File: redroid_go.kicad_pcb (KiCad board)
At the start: 2 copper layers, 70 x 95 mm, 100 parts, among them J1 USB4105-GF-A, J2 5051101892, J3 Conn_01x02_Pin, J4 Conn_01x10_Pin, Q1 UMH3N, Q2 PMOS, Q3 UMH3N, SW1 UP, SW10 A, SW11 SW_SPDT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

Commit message: Change DPAD resistors
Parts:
- R11, R12, R13, R14: value 10k -> 100k
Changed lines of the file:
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@@
 			)
 		)
-		(property "Value" "10k"
+		(property "Value" "100k"
 			(at 0 -1.43 0)
 			(layer "B.Fab")
@@
 			)
 		)
-		(property "Value" "10k"
+		(property "Value" "100k"
 			(at 0 -1.43 0)
 			(layer "B.Fab")
@@
 			)
 		)
-		(property "Value" "10k"
+		(property "Value" "100k"
 			(at 0 -1.43 0)
 			(layer "B.Fab")
@@
 			)
 		)
-		(property "Value" "10k"
+		(property "Value" "100k"
 			(at 0 -1.43 0)
 			(layer "B.Fab")

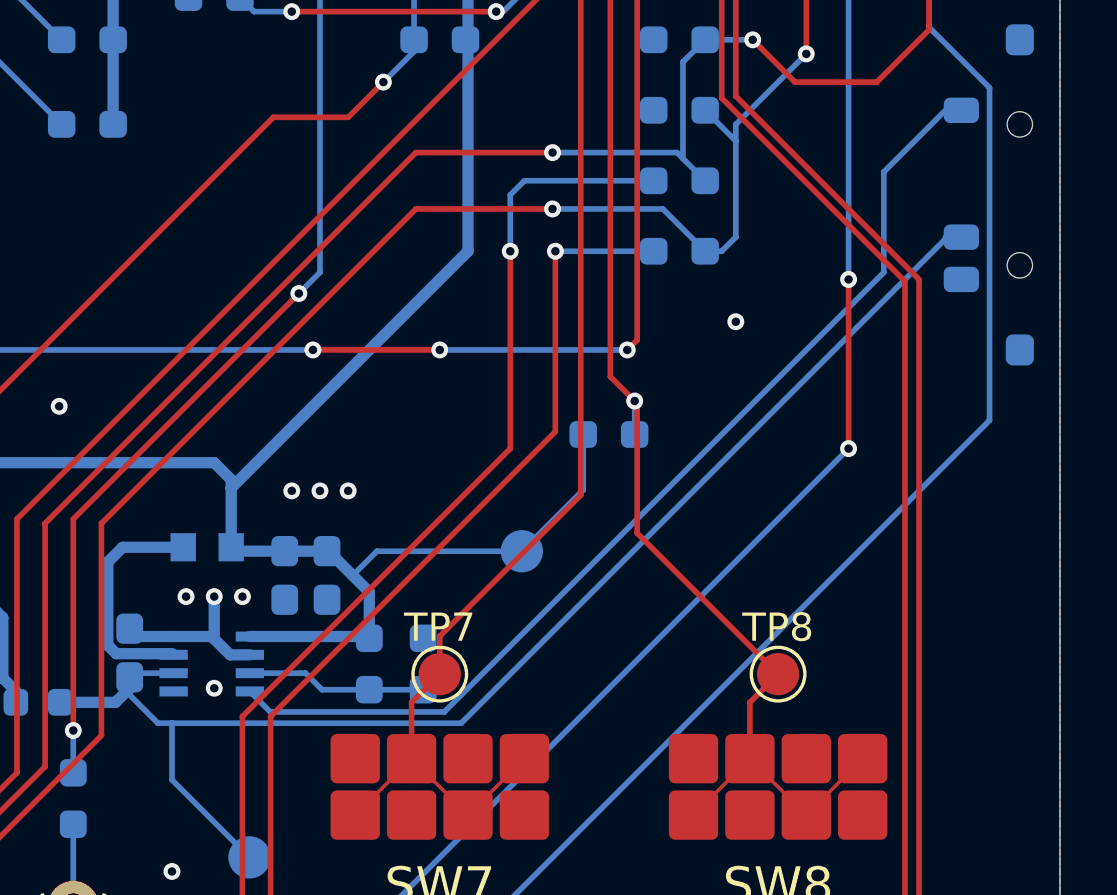
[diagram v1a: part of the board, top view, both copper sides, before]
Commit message: Fix filled zones
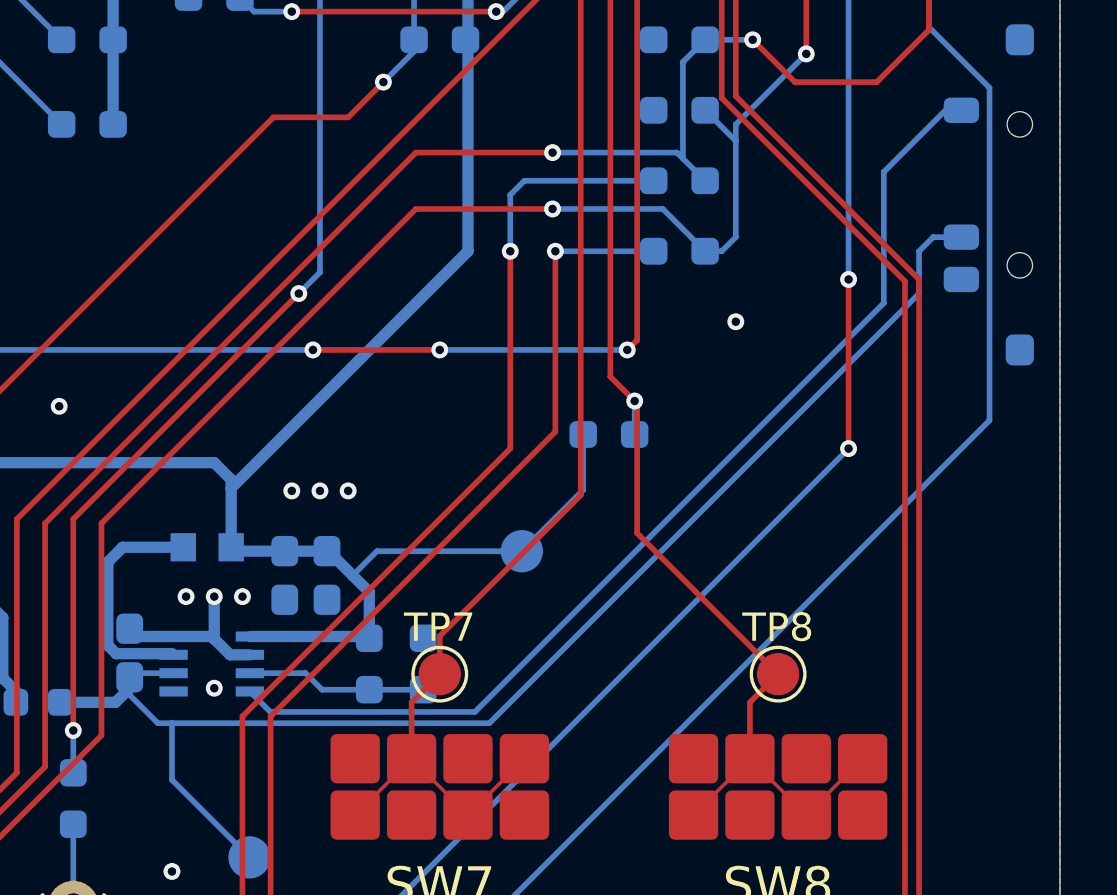
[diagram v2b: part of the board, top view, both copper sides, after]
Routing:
- net Net-(SW11-B): track 47.7 -> 49.1 mm
- net Net-(SW11-A): track 35.9 -> 36.5 mm
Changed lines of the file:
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@@
 	)
 	(segment
-		(start 194.4375 85.5625)
-		(end 177.259551 102.740449)
+		(start 178.259551 102.740449)
+		(end 167 102.740449)
 		(width 0.2)
 		(layer "B.Cu")
@@
 	)
 	(segment
-		(start 177.259551 102.740449)
+		(start 167 104.75)
 		(end 167 102.740449)
 		(width 0.2)
@@
 	)
 	(segment
-		(start 167 104.75)
-		(end 167 102.740449)
+		(start 193.5 86)
+		(end 193.5 87.5)
 		(width 0.2)
 		(layer "B.Cu")
@@
 	)
 	(segment
+		(start 195 85.5)
+		(end 194 85.5)
+		(width 0.2)
+		(layer "B.Cu")
+		(net 4)
+	)
+	(segment
 		(start 167.057201 100.96545)
 		(end 165.64705 100.96545)
@@
 	)
 	(segment
-		(start 194.4375 85.5)
-		(end 194.4375 85.5625)
+		(start 165.64705 100.96545)
+		(end 165.5 101.1125)
 		(width 0.2)
 		(layer "B.Cu")
@@
 	)
 	(segment
-		(start 165.64705 100.96545)
-		(end 165.5 101.1125)
+		(start 193.5 87.5)
+		(end 178.259551 102.740449)
 		(width 0.2)
 		(layer "B.Cu")
@@
 	)
 	(segment
+		(start 194 85.5)
+		(end 193.5 86)
+		(width 0.2)
+		(layer "B.Cu")
+		(net 4)
+	)
+	(segment
 		(start 136.5 52)
 		(end 137 51.5)
@@
 	)
 	(segment
-		(start 192.25 83.1875)
-		(end 192.25 86.75)
+		(start 177.746934 102.340449)
+		(end 170.488698 102.340449)
 		(width 0.2)
 		(layer "B.Cu")
@@
 	)
 	(segment
-		(start 170.488698 102.340449)
-		(end 169.763697 101.615448)
+		(start 194.4375 81)
+		(end 192.25 83.1875)
 		(width 0.2)
 		(layer "B.Cu")
@@
 	)
 	(segment
-		(start 192.25 86.75)
-		(end 176.659551 102.340449)
+		(start 170.488698 102.340449)
+		(end 169.763697 101.615448)
 		(width 0.2)
 		(layer "B.Cu")
@@
 	)
 	(segment
-		(start 194.4375 81)
-		(end 192.25 83.1875)
+		(start 192.25 87.837383)
+		(end 177.746934 102.340449)
 		(width 0.2)
 		(layer "B.Cu")
@@
 	)
 	(segment
-		(start 176.659551 102.340449)
-		(end 170.488698 102.340449)
+		(start 192.25 83.1875)
+		(end 192.25 87.837383)
 		(width 0.2)
 		(layer "B.Cu")

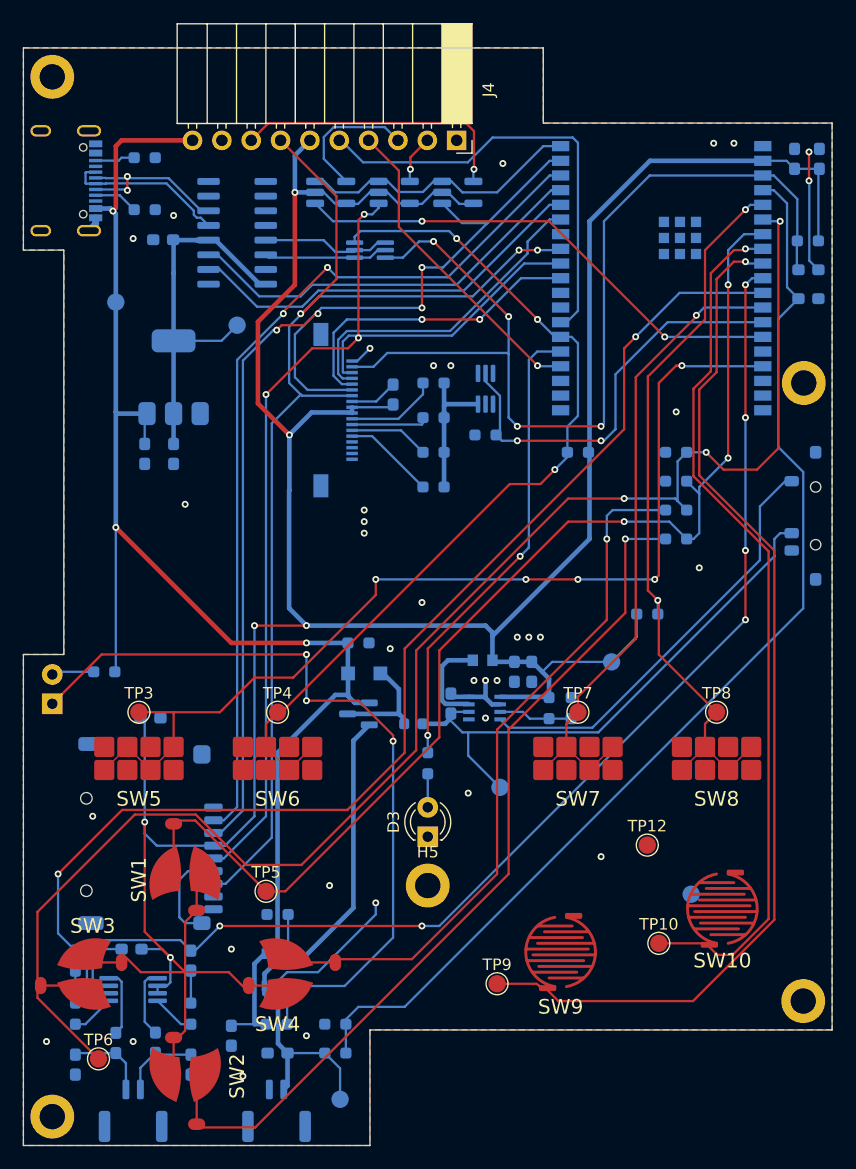
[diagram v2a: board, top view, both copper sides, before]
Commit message: Move menu buttons
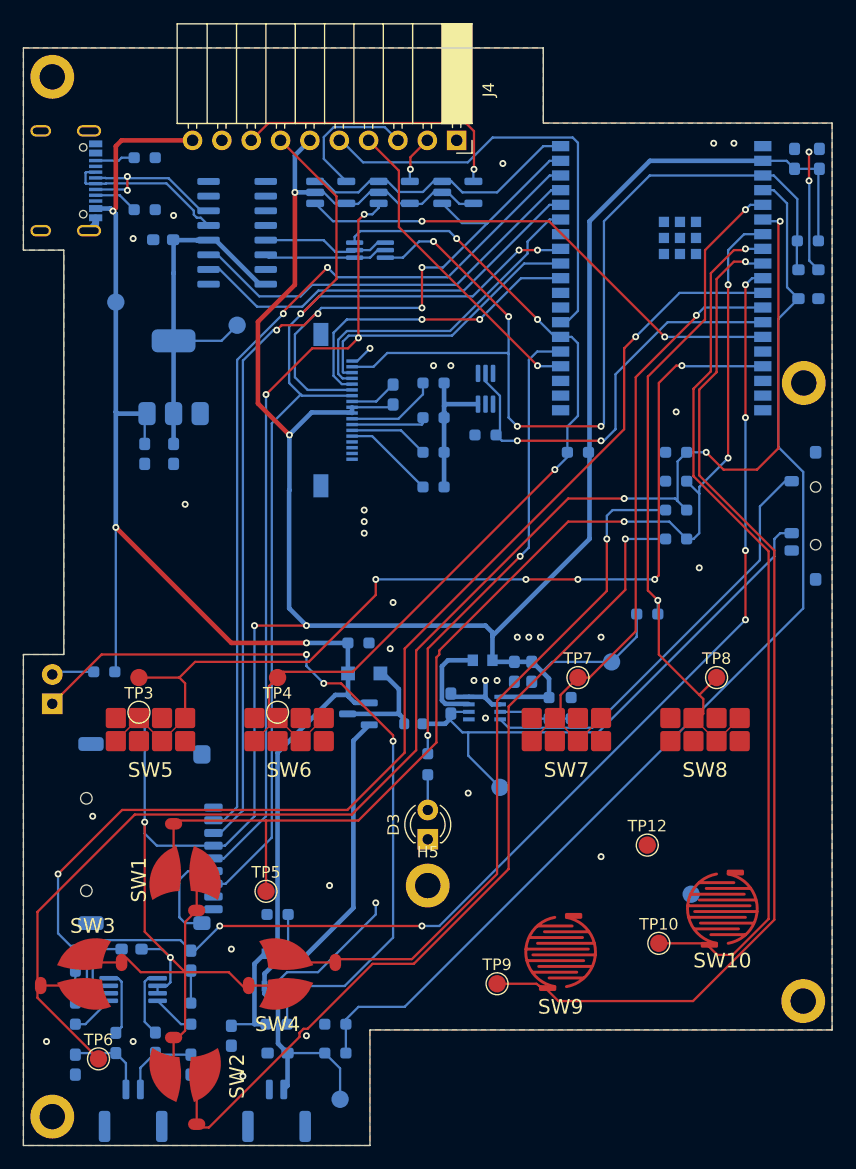
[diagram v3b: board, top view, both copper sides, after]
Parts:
- moved TP7 3.00 mm to (176.5, 98.0)
- moved TP8 3.00 mm to (188.5, 98.0)
- moved SW5 2.69 mm to (139.5, 102.5)
- moved SW6 2.69 mm to (151.5, 102.5)
- moved SW7 2.69 mm to (175.5, 102.5)
- moved SW8 2.69 mm to (187.5, 102.5)
- moved D3 0.23 mm to (163.5, 112.0)
- moved R18 0.09 mm to (163.5, 105.5)
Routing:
- net IO34: track 129.6 -> 126.0 mm
- net Net-(D2-K): track 68.3 -> 66.5 mm
- net IO27: track 47.9 -> 46.2 mm
- net IO0: track 72.2 -> 70.8 mm
- net IO39: track 55.6 -> 54.3 mm
- net IO35: track 96.9 -> 98.1 mm
- net IO13: track 79.8 -> 79.3 mm
- net GND: vias 35 -> 36

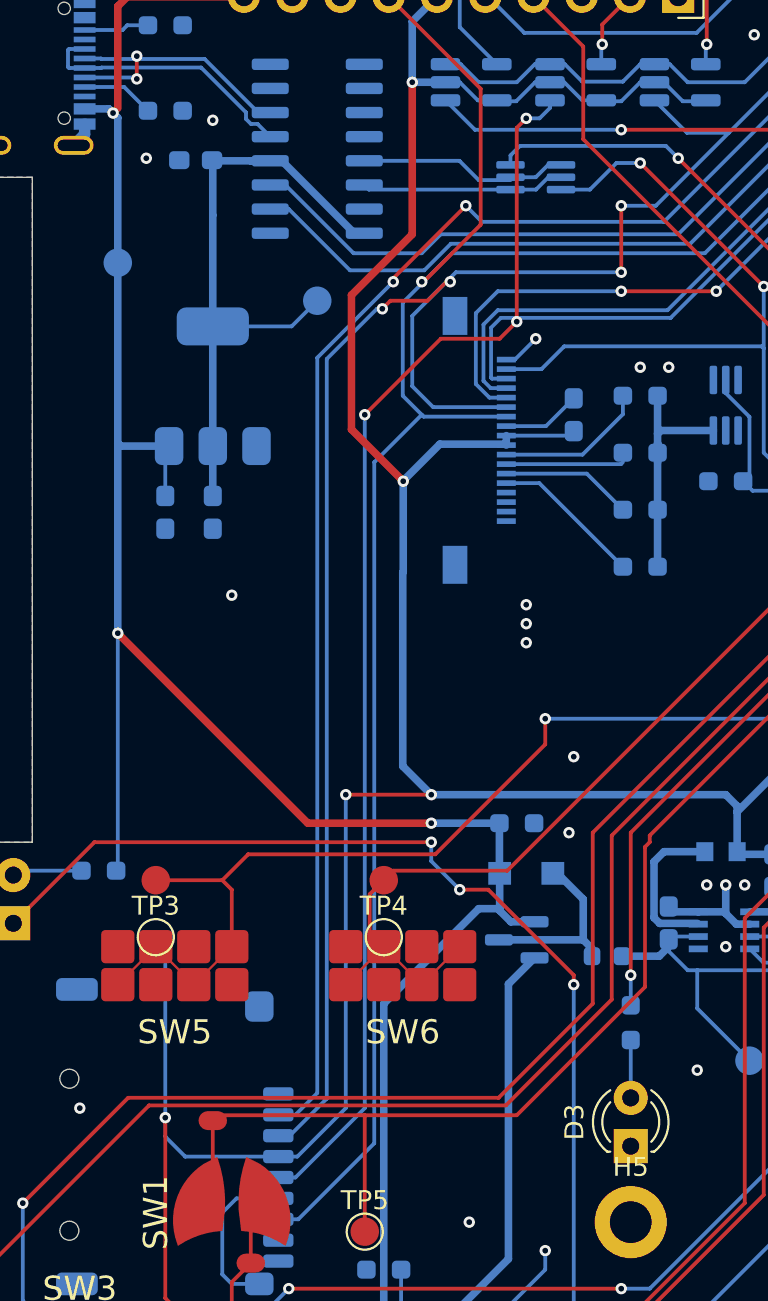
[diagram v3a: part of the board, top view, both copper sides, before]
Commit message: Change serial LDO to SOT23-3 and update BOM
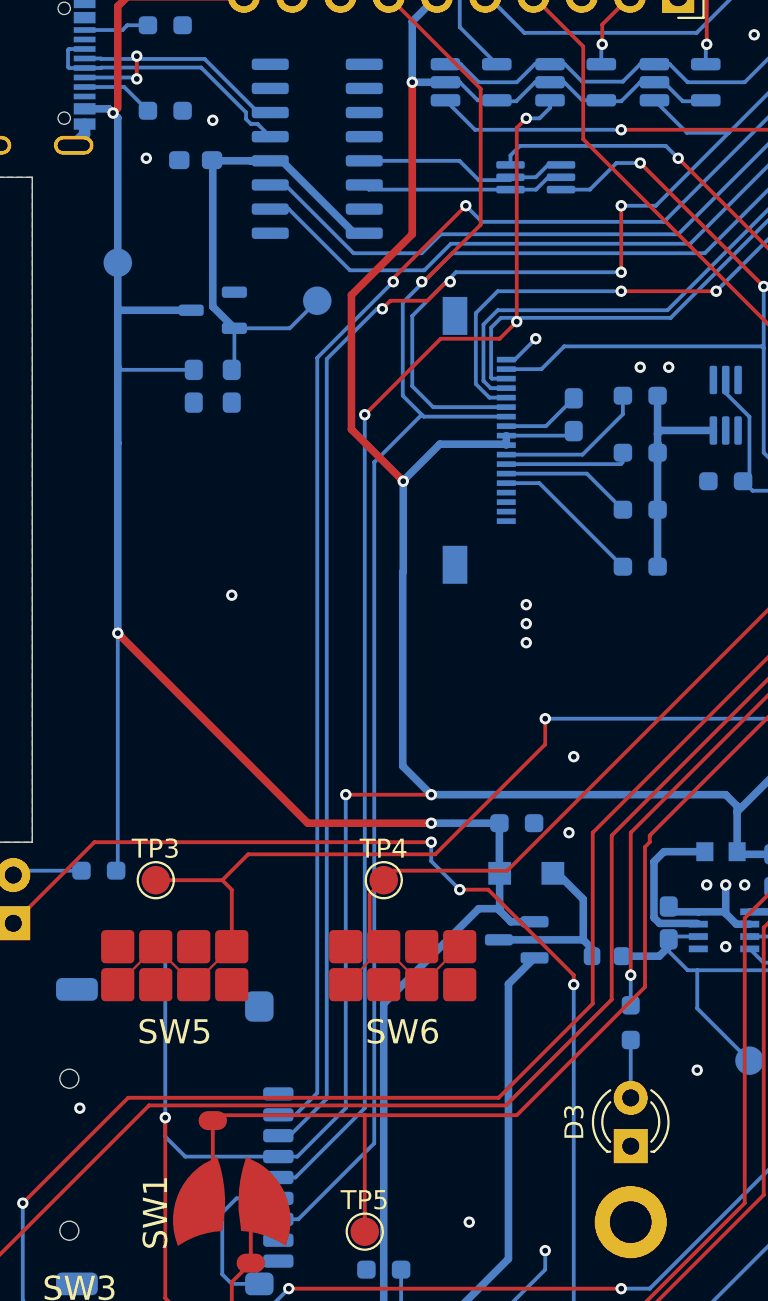
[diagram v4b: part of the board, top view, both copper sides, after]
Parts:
- U5: value AMS1117-3.3 -> XC6206PxxxMR; footprint Package_TO_SOT_SMD:SOT-223-3_TabPin2 -> Package_TO_SOT_SMD:SOT-23-3
- moved C17 6.80 mm to (140.5, 72.0)
- moved C18 6.71 mm to (142.5, 72.0)
- moved U5 4.00 mm to (141.5, 68.0), turned to 180 degrees
- moved TP3 3.00 mm to (138.5, 98.0)
- moved TP4 3.00 mm to (150.5, 98.0)
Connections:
- net IO21 renamed D/C
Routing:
- net P3V3_SERIAL: track 35.6 -> 28.4 mm
- net VBUS: track 126.4 -> 128.9 mm

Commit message: Minor fixes in PCB
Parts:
- moved TP1 2.67 mm to (177.0, 95.5)
- moved SW11 1.50 mm to (202.5, 82.5)
- moved TP3 1.00 mm to (139.5, 98.0)
- moved TP4 1.00 mm to (151.5, 98.0)
- moved TP7 1.00 mm to (175.5, 98.0)
- moved TP8 1.00 mm to (187.5, 98.0)
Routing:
- net GND: track 76.5 -> 65.4 mm, vias 36 -> 35
- net MOSI: track 94.9 -> 91.0 mm
- net IO13: track 79.3 -> 77.3 mm
- net Net-(SW11-B): track 49.1 -> 47.6 mm
- net Net-(SW11-A): track 36.5 -> 35.3 mm
- net P3V3: track 268.4 -> 269.5 mm
- net IO39: track 54.3 -> 53.2 mm
- net IO25: track 105.5 -> 106.4 mm
- net VBUS: track 128.9 -> 128.0 mm
- net CS1: track 76.6 -> 75.9 mm
- net IO27: track 46.2 -> 46.9 mm
- net IO0: track 70.8 -> 70.2 mm

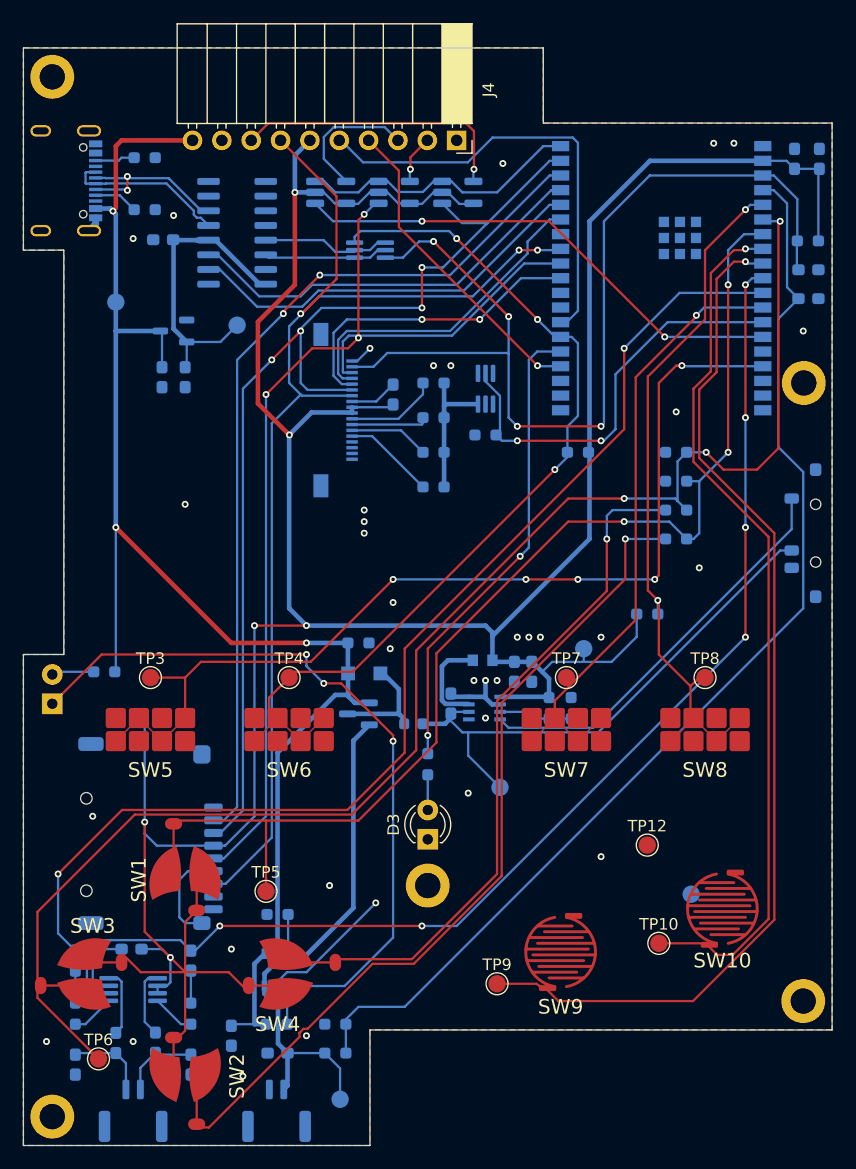
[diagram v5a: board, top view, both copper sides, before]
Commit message: Adjust DPAD and menu buttons pad position
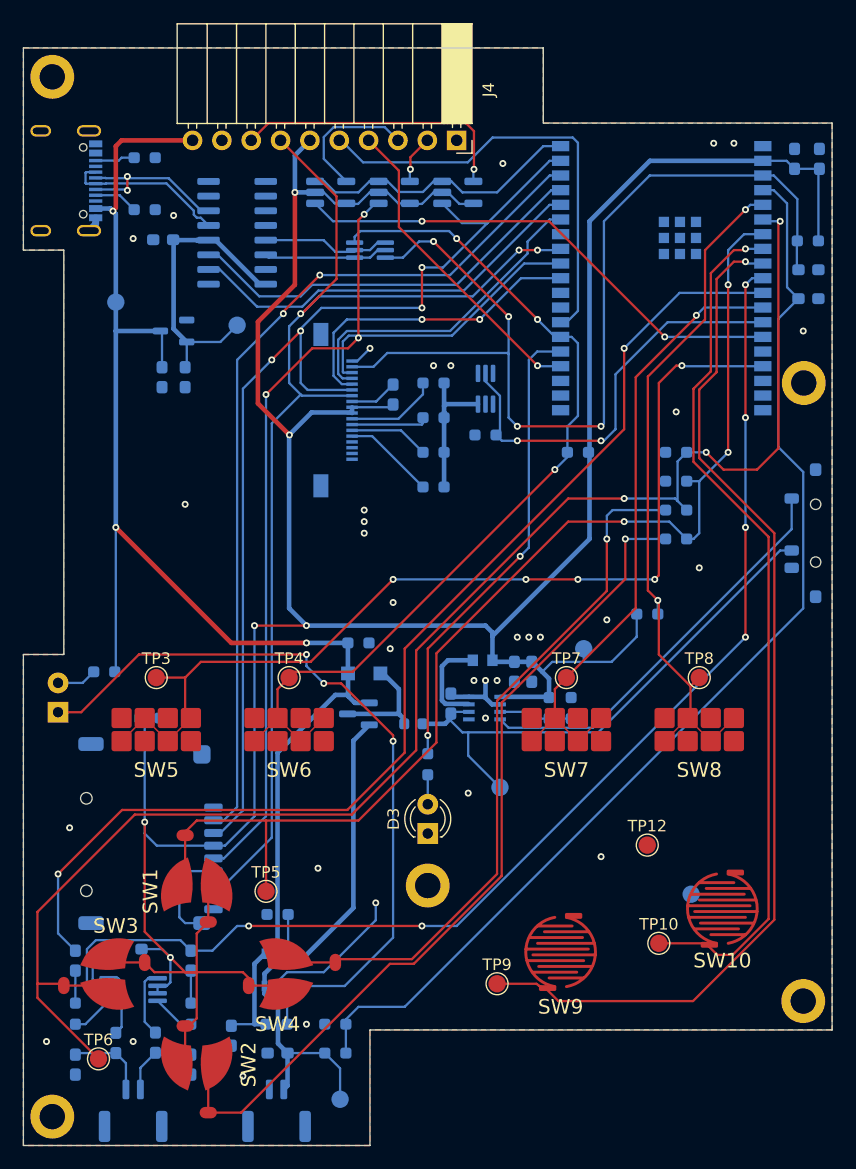
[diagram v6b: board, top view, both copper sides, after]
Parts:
- moved SW3 2.00 mm to (136.5, 123.7)
- moved SW1 1.41 mm to (143.5, 116.7)
- moved SW2 1.41 mm to (143.5, 130.7)
- moved D2 0.88 mm to (131.5, 101.0)
- moved D3 0.50 mm to (163.5, 111.5)
- moved SW5 0.50 mm to (140.0, 102.5)
- moved SW8 0.50 mm to (187.0, 102.5)
- moved TP3 0.50 mm to (140.0, 98.0)
- moved TP8 0.50 mm to (187.0, 98.0)
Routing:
- net P3V3: track 269.5 -> 266.8 mm
- net IO34: track 126.0 -> 128.6 mm
- net Net-(R11-Pad2): track 72.4 -> 70.6 mm
- net IO27: track 46.9 -> 45.5 mm
- net GND: track 65.4 -> 66.3 mm, vias 35 -> 34
